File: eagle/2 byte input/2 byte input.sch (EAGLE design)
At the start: 26 parts, among them IC1 74LS165N, IC2 74LS165N, X1 MKDSN1,5/5-5,08, X2 MKDSN1,5/5-5,08, X3 MKDSN1,5/8-5,08, X5 MKDSN1,5/8-5,08

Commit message: check in changes
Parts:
- R9: value (none) -> 10K
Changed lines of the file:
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@@
 <part name="R7" library="resistor" library_urn="urn:adsk.eagle:library:348" deviceset="R-US_" device="0207/2V" package3d_urn="urn:adsk.eagle:package:23490/1"/>
 <part name="R8" library="resistor" library_urn="urn:adsk.eagle:library:348" deviceset="R-US_" device="0207/2V" package3d_urn="urn:adsk.eagle:package:23490/1"/>
-<part name="R9" library="resistor" library_urn="urn:adsk.eagle:library:348" deviceset="R-US_" device="0207/2V" package3d_urn="urn:adsk.eagle:package:23490/1"/>
+<part name="R9" library="resistor" library_urn="urn:adsk.eagle:library:348" deviceset="R-US_" device="0207/2V" package3d_urn="urn:adsk.eagle:package:23490/1" value="10K"/>
 <part name="R10" library="resistor" library_urn="urn:adsk.eagle:library:348" deviceset="R-US_" device="0207/2V" package3d_urn="urn:adsk.eagle:package:23490/1"/>
 <part name="R11" library="resistor" library_urn="urn:adsk.eagle:library:348" deviceset="R-US_" device="0207/2V" package3d_urn="urn:adsk.eagle:package:23490/1"/>

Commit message: corrected circuit for input board
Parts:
- removed X1, X2: MKDSN1,5/5-5,08, con-phoenix-508:MKDSN1,5/5-5,08
- added JP1, JP2: (no value), pinhead:PINHD-1X6/90
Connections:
- removed net SER0: IC1A.SER, X1-4.KL
- removed net SER1: IC1A.QH, IC2A.SER
- removed net SERX: IC2A.QH, X2-4.KL
- new net CE: IC1A.INH, IC2A.INH, JP1.4, JP2.3
- new net S0: IC1A.QH, JP1.5
- new net S1: IC1A.SER, IC2A.QH
- new net SX: IC2A.SER, JP2.2
- net +5V: now also JP1.6, JP2.1; no longer X1-1.KL, X2-1.KL
- net CLK: now also JP1.3, JP2.4; no longer X1-3.KL, X2-3.KL
- net GND: now also JP1.1, JP2.6; no longer IC1A.INH, IC2A.INH, X1-5.KL, X2-5.KL
- net LATCH: now also JP1.2, JP2.5; no longer X1-2.KL, X2-2.KL

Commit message: periodic check-in
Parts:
- R9: value 10K -> 4K7
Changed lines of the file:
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@@
 <part name="R7" library="resistor" library_urn="urn:adsk.eagle:library:348" deviceset="R-US_" device="0207/2V" package3d_urn="urn:adsk.eagle:package:23490/1"/>
 <part name="R8" library="resistor" library_urn="urn:adsk.eagle:library:348" deviceset="R-US_" device="0207/2V" package3d_urn="urn:adsk.eagle:package:23490/1"/>
-<part name="R9" library="resistor" library_urn="urn:adsk.eagle:library:348" deviceset="R-US_" device="0207/2V" package3d_urn="urn:adsk.eagle:package:23490/1" value="10K"/>
+<part name="R9" library="resistor" library_urn="urn:adsk.eagle:library:348" deviceset="R-US_" device="0207/2V" package3d_urn="urn:adsk.eagle:package:23490/1" value="4K7"/>
 <part name="R10" library="resistor" library_urn="urn:adsk.eagle:library:348" deviceset="R-US_" device="0207/2V" package3d_urn="urn:adsk.eagle:package:23490/1"/>
 <part name="R11" library="resistor" library_urn="urn:adsk.eagle:library:348" deviceset="R-US_" device="0207/2V" package3d_urn="urn:adsk.eagle:package:23490/1"/>

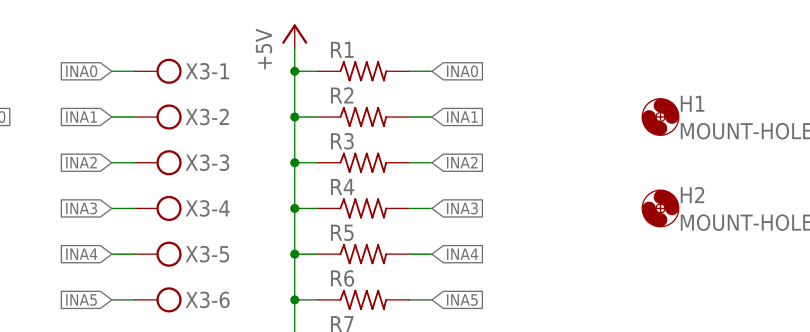
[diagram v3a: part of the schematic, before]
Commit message: added pdf file of schematics and boards, removed button debounce and servo driver
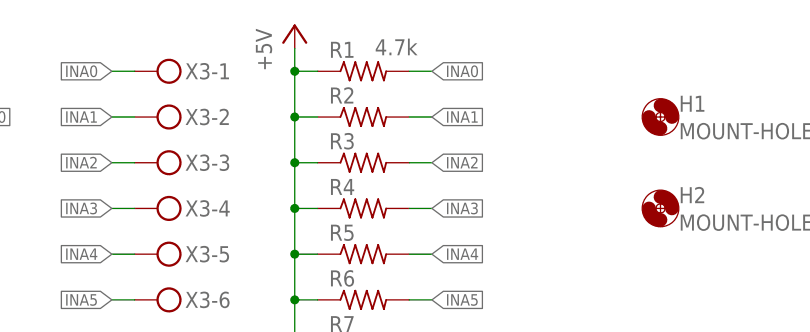
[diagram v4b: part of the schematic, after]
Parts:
- R1: value (none) -> 4.7k
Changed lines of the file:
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@@
 <?xml version="1.0" encoding="utf-8"?>
 <!DOCTYPE eagle SYSTEM "eagle.dtd">
-<eagle version="9.4.2">
+<eagle version="9.5.0">
 <drawing>
 <settings>
@@
 <part name="C1" library="resistor" library_urn="urn:adsk.eagle:library:348" deviceset="C-US" device="025-025X050" package3d_urn="urn:adsk.eagle:package:23629/2" value="0.1uf"/>
 <part name="C2" library="resistor" library_urn="urn:adsk.eagle:library:348" deviceset="C-US" device="025-025X050" package3d_urn="urn:adsk.eagle:package:23629/2" value="0.1uf"/>
-<part name="R1" library="resistor" library_urn="urn:adsk.eagle:library:348" deviceset="R-US_" device="0207/2V" package3d_urn="urn:adsk.eagle:package:23490/1"/>
+<part name="R1" library="resistor" library_urn="urn:adsk.eagle:library:348" deviceset="R-US_" device="0207/2V" package3d_urn="urn:adsk.eagle:package:23490/1" value="4.7k"/>
 <part name="R2" library="resistor" library_urn="urn:adsk.eagle:library:348" deviceset="R-US_" device="0207/2V" package3d_urn="urn:adsk.eagle:package:23490/1"/>
 <part name="R3" library="resistor" library_urn="urn:adsk.eagle:library:348" deviceset="R-US_" device="0207/2V" package3d_urn="urn:adsk.eagle:package:23490/1"/>
@@
 <part name="JP1" library="pinhead" library_urn="urn:adsk.eagle:library:325" deviceset="PINHD-1X6" device="/90" package3d_urn="urn:adsk.eagle:package:22475/2"/>
 <part name="JP2" library="pinhead" library_urn="urn:adsk.eagle:library:325" deviceset="PINHD-1X6" device="/90" package3d_urn="urn:adsk.eagle:package:22475/2"/>
+<part name="FRAME1" library="frames" library_urn="urn:adsk.eagle:library:229" deviceset="LETTER_L" device=""/>
 </parts>
 <sheets>
@@
 <instance part="R1" gate="G$1" x="58.42" y="96.52" smashed="yes">
 <attribute name="NAME" x="54.61" y="98.0186" size="1.778" layer="95"/>
-<attribute name="VALUE" x="54.61" y="93.218" size="1.778" layer="96"/>
+<attribute name="VALUE" x="59.69" y="98.298" size="1.778" layer="96"/>
 </instance>
 <instance part="R2" gate="G$1" x="58.42" y="91.44" smashed="yes">
@@
 <attribute name="VALUE" x="120.65" y="22.86" size="1.778" layer="96"/>
 </instance>
+<instance part="FRAME1" gate="G$1" x="-73.66" y="-55.88" smashed="yes"/>
+<instance part="FRAME1" gate="G$2" x="73.66" y="-55.88" smashed="yes">
+<attribute name="LAST_DATE_TIME" x="86.36" y="-54.61" size="2.54" layer="94"/>
+<attribute name="SHEET" x="160.02" y="-54.61" size="2.54" layer="94"/>
+<attribute name="DRAWING_NAME" x="91.44" y="-36.83" size="2.54" layer="94"/>
+</instance>
 </instances>
